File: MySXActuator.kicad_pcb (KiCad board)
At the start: 2 copper layers, 26.4 x 38.1 mm, 23 parts, among them Q1 2N7002, Q2 IRF530, Q3 IRF530, Q4 2N7002, U1 AP63205WU, X1 FE10-2, X2 MKDSN1,5/6-5,08

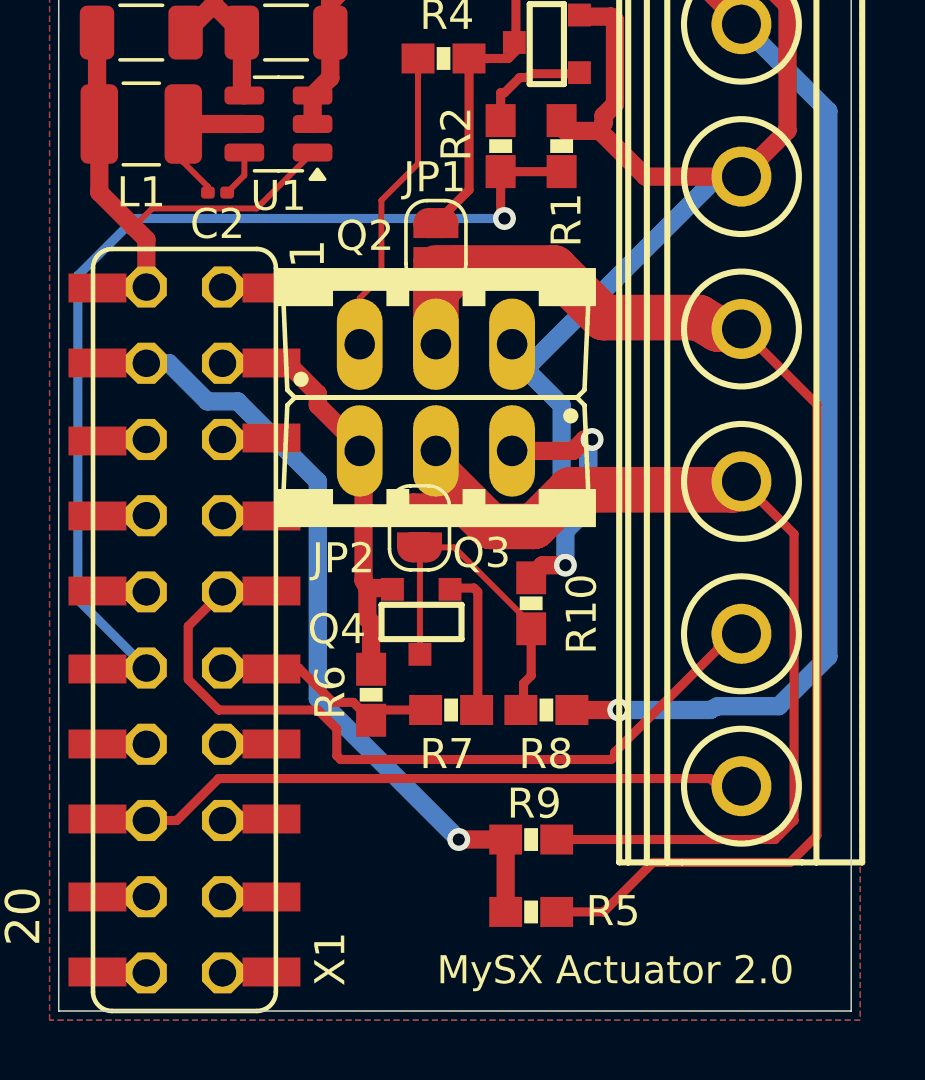
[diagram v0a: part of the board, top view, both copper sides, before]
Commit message: change C2 footprint from 0201 to 0402
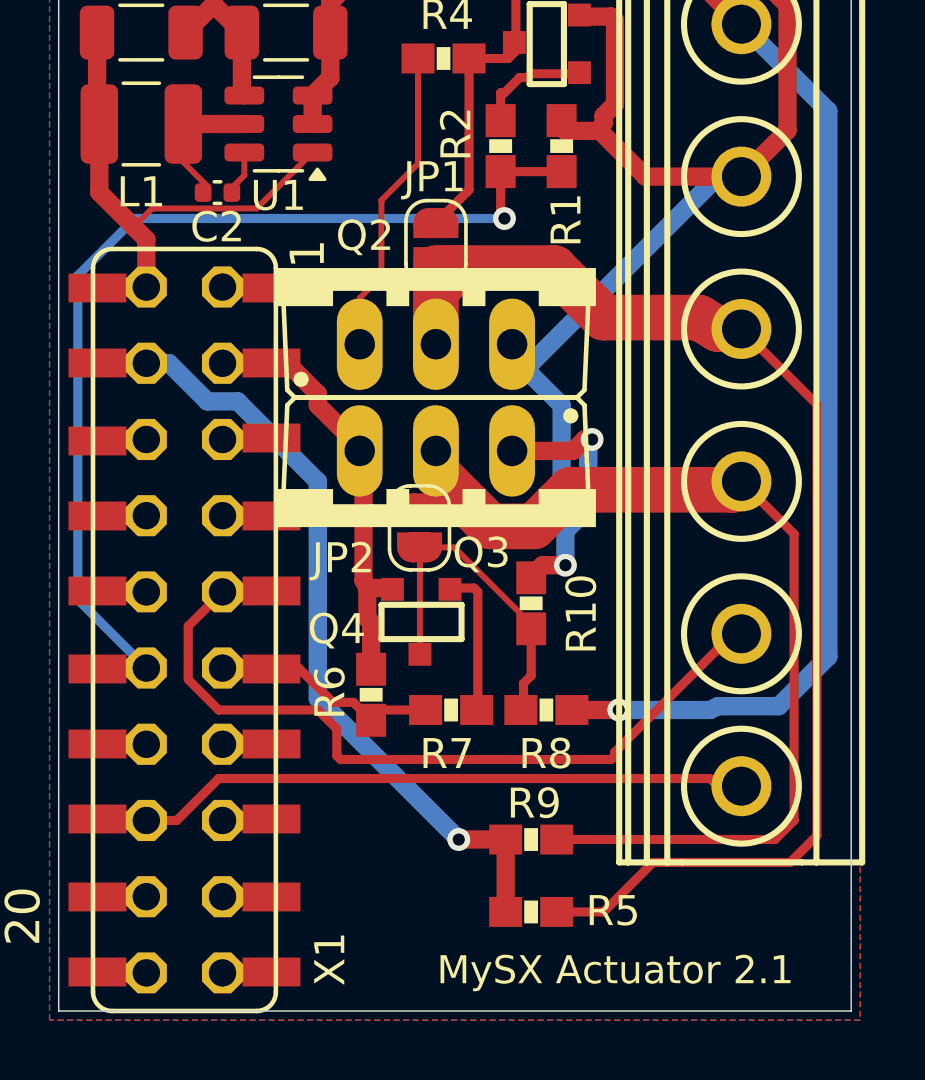
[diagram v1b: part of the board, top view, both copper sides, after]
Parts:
- C2: footprint Capacitor_SMD:C_0201_0603Metric -> Capacitor_SMD:C_0402_1005Metric
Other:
- board text added: "MySX Actuator 2.1"
- board text removed: "MySX Actuator 2.0"
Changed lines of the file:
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@@
       (net 9 "Net-(JP2-A)") (pinfunction "2") (pintype "passive") (solder_mask_margin 0.0762) (thermal_bridge_angle 0))
   )
-  (footprint "Capacitor_SMD:C_0201_0603Metric" (layer "F.Cu")
+  (footprint "Capacitor_SMD:C_0402_1005Metric" (layer "F.Cu")
     (at 140.586 96.774 180)
-    (descr "Capacitor SMD 0201 (0603 Metric), square (rectangular) end terminal, IPC_7351 nominal, (Body size source: https://www.vishay.com/docs/20052/crcw0201e3.pdf), generated with kicad-footprint-generator")
+    (descr "Capacitor SMD 0402 (1005 Metric), square (rectangular) end terminal, IPC_7351 nominal, (Body size source: IPC-SM-782 page 76, https://www.pcb-3d.com/wordpress/wp-content/uploads/ipc-sm-782a_amendment_1_and_2.pdf), generated with kicad-footprint-generator")
     (tags "capacitor")
     (property "Sheetfile" "MySXActuator.kicad_sch")
@@
     (property "ki_keywords" "cap capacitor")
     (attr smd)
-    (fp_text reference "C2" (at 0 -1.05) (layer "F.SilkS")
+    (fp_text reference "C2" (at 0 -1.16 180) (layer "F.SilkS")
         (effects (font (size 1 1) (thickness 0.15)))
     )
-    (fp_text value "100n" (at 0 1.05) (layer "F.Fab")
+    (fp_text value "100n" (at 0 1.16 180) (layer "F.Fab")
         (effects (font (size 1 1) (thickness 0.15)))
     )
-    (fp_text user "${REFERENCE}" (at 0 -0.68) (layer "F.Fab")
+    (fp_text user "${REFERENCE}" (at 0 0 180) (layer "F.Fab")
         (effects (font (size 0.25 0.25) (thickness 0.04)))
     )
-    (fp_line (start -0.7 -0.35) (end 0.7 -0.35)
-      (stroke (width 0.05) (type solid)) (layer "F.CrtYd"))
-    (fp_line (start -0.7 0.35) (end -0.7 -0.35)
-      (stroke (width 0.05) (type solid)) (layer "F.CrtYd"))
-    (fp_line (start 0.7 -0.35) (end 0.7 0.35)
-      (stroke (width 0.05) (type solid)) (layer "F.CrtYd"))
-    (fp_line (start 0.7 0.35) (end -0.7 0.35)
-      (stroke (width 0.05) (type solid)) (layer "F.CrtYd"))
-    (fp_line (start -0.3 -0.15) (end 0.3 -0.15)
-      (stroke (width 0.1) (type solid)) (layer "F.Fab"))
-    (fp_line (start -0.3 0.15) (end -0.3 -0.15)
-      (stroke (width 0.1) (type solid)) (layer "F.Fab"))
-    (fp_line (start 0.3 -0.15) (end 0.3 0.15)
-      (stroke (width 0.1) (type solid)) (layer "F.Fab"))
-    (fp_line (start 0.3 0.15) (end -0.3 0.15)
-      (stroke (width 0.1) (type solid)) (layer "F.Fab"))
-    (pad "" smd roundrect (at -0.345 0 180) (size 0.318 0.36) (layers "F.Paste") (roundrect_rratio 0.25))
-    (pad "" smd roundrect (at 0.345 0 180) (size 0.318 0.36) (layers "F.Paste") (roundrect_rratio 0.25))
-    (pad "1" smd roundrect (at -0.32 0 180) (size 0.46 0.4) (layers "F.Cu" "F.Mask") (roundrect_rratio 0.25)
+    (fp_line (start -0.107836 -0.36) (end 0.107836 -0.36)
+      (stroke (width 0.12) (type solid)) (layer "F.SilkS"))
+    (fp_line (start -0.107836 0.36) (end 0.107836 0.36)
+      (stroke (width 0.12) (type solid)) (layer "F.SilkS"))
+    (fp_line (start -0.91 -0.46) (end 0.91 -0.46)
+      (stroke (width 0.05) (type solid)) (layer "F.CrtYd"))
+    (fp_line (start -0.91 0.46) (end -0.91 -0.46)
+      (stroke (width 0.05) (type solid)) (layer "F.CrtYd"))
+    (fp_line (start 0.91 -0.46) (end 0.91 0.46)
+      (stroke (width 0.05) (type solid)) (layer "F.CrtYd"))
+    (fp_line (start 0.91 0.46) (end -0.91 0.46)
+      (stroke (width 0.05) (type solid)) (layer "F.CrtYd"))
+    (fp_line (start -0.5 -0.25) (end 0.5 -0.25)
+      (stroke (width 0.1) (type solid)) (layer "F.Fab"))
+    (fp_line (start -0.5 0.25) (end -0.5 -0.25)
+      (stroke (width 0.1) (type solid)) (layer "F.Fab"))
+    (fp_line (start 0.5 -0.25) (end 0.5 0.25)
+      (stroke (width 0.1) (type solid)) (layer "F.Fab"))
+    (fp_line (start 0.5 0.25) (end -0.5 0.25)
+      (stroke (width 0.1) (type solid)) (layer "F.Fab"))
+    (pad "1" smd roundrect (at -0.48 0 180) (size 0.56 0.62) (layers "F.Cu" "F.Paste" "F.Mask") (roundrect_rratio 0.25)
       (net 29 "Net-(U1-BST)") (pintype "passive"))
-    (pad "2" smd roundrect (at 0.32 0 180) (size 0.46 0.4) (layers "F.Cu" "F.Mask") (roundrect_rratio 0.25)
+    (pad "2" smd roundrect (at 0.48 0 180) (size 0.56 0.62) (layers "F.Cu" "F.Paste" "F.Mask") (roundrect_rratio 0.25)
       (net 30 "Net-(U1-SW)") (pintype "passive"))
-    (model "${KICAD6_3DMODEL_DIR}/Capacitor_SMD.3dshapes/C_0201_0603Metric.wrl"
+    (model "${KICAD6_3DMODEL_DIR}/Capacitor_SMD.3dshapes/C_0402_1005Metric.wrl"
       (offset (xyz 0 0 0))
       (scale (xyz 1 1 1))
@@
   (gr_line (start 161.7091 85.9536) (end 135.2931 85.9536)
     (stroke (width 0.05) (type solid)) (layer "Edge.Cuts"))
-  (gr_text "MySX Actuator 2.0" (at 159.8041 122.1486) (layer "F.SilkS")
+  (gr_text "MySX Actuator 2.1" (at 159.8041 122.1486) (layer "F.SilkS")
     (effects (font (size 0.93472 0.93472) (thickness 0.08128)) (justify right top))
   )

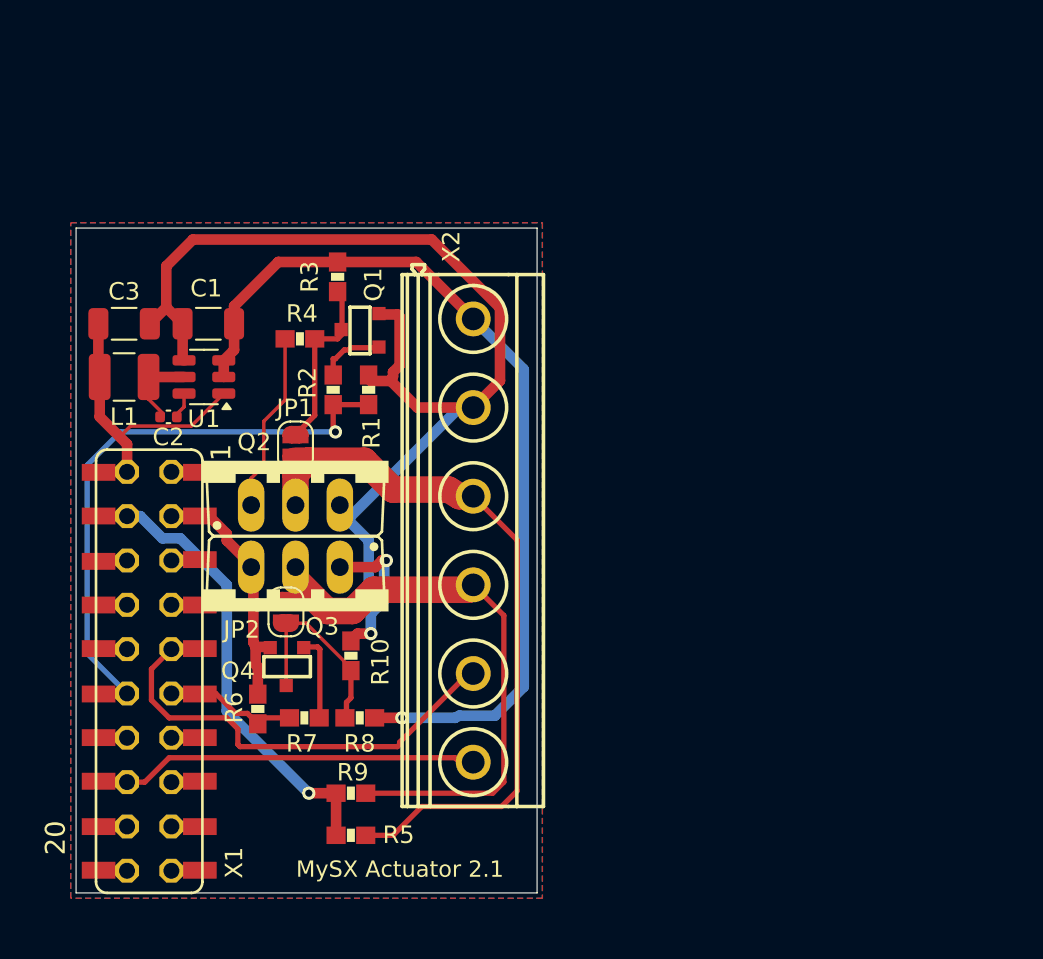
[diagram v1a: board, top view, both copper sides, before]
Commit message: refactor schematic to use kicad native symbols and footprints
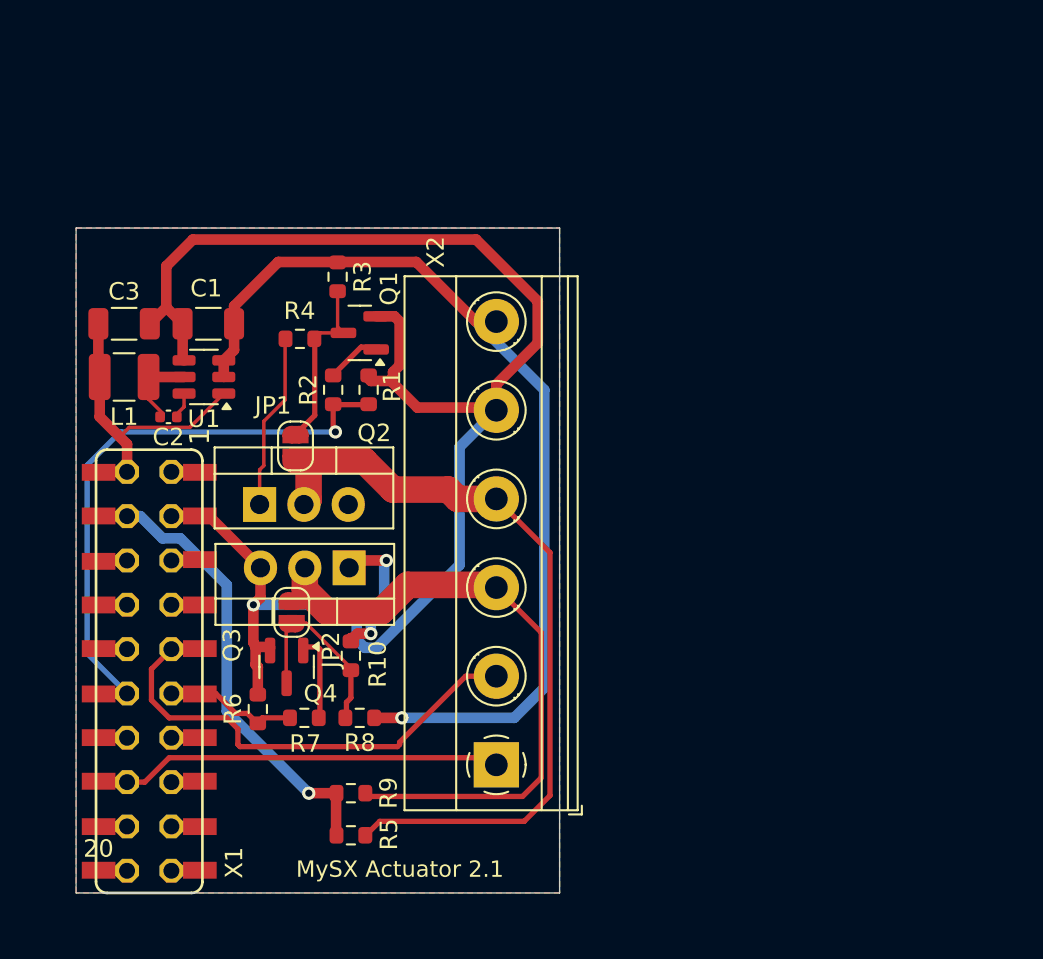
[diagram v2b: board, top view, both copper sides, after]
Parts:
- C1: value 10u -> 10u/50V
- Q1, Q4: footprint MySXActuator:SOT-23 -> Package_TO_SOT_SMD:SOT-23
- Q2, Q3: value IRF530 -> IRF540N; footprint MySXActuator:TO220BV -> Package_TO_SOT_THT:TO-220-3_Vertical
- R1, R10, R2, R3, R4, R5, R6, R7, R8, R9: footprint MySXActuator:0603-RES -> Resistor_SMD:R_0603_1608Metric
- X1: value FE10-2 -> ~
- X2: value MKDSN1,5/6-5,08 -> ~; footprint MySXActuator:MKDSN1,5_6-5,08 -> TerminalBlock_Phoenix:TerminalBlock_Phoenix_MKDS-1,5-6-5.08_1x06_P5.08mm_Horizontal
- moved X2 12.9 mm to (159.4, 116.7), turned to 90 degrees
- moved Q3 3.96 mm to (150.9, 105.4)
- moved Q2 3.24 mm to (145.8, 101.8)
- moved JP2 0.33 mm to (147.7, 108.0)
- moved Q1 0.17 mm to (151.5, 92.0), turned to 180 degrees
- turned Q4 to -90 degrees
- turned R1 to 90 degrees
- turned R10 to 90 degrees
- turned R3 to -90 degrees
- turned R4 to 180 degrees
- turned R5 to 0 degrees
- turned R6 to 90 degrees
- turned R8 to 180 degrees
- turned R9 to 0 degrees
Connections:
- net /D10_A4 renamed D10_A4
- net /D11_MOSI renamed D11_MOSI
- net /D12_MISO renamed D12_MISO
- net /D13_SCK renamed D13_SCK
- net /D14_CS renamed D14_CS
- net /D1_TX renamed D1_TX
- net /D2_RX renamed D3_RX
- net /D3_INT renamed D3_INT
- net /D7_SCL renamed D7_SCL
- net /D8_SDA renamed D8_SDA
- net /LEGACY_ID renamed LEGACY_ID
- net /RST renamed RST
- net /VCC renamed VCC
- net /VRAW renamed VRAW
- C1 pad 1: /Vin -> VIN
- JP1 pad 2: /LED1 -> LED1
- JP2 pad 2: /LED2 -> LED2
- R1 pad 1: GND -> D5_PWM
- R1 pad 2: /D5_PWM -> GND
- R10 pad 1: Net-(Q3-PadG) -> Net-(JP2-A)
- R10 pad 2: Net-(JP2-A) -> Net-(Q3-G)
- R2 pad 1: /D5_PWM -> D5_PWM
- R3 pad 1: Net-(JP1-A) -> VIN
- R3 pad 2: /Vin -> Net-(JP1-A)
- R4 pad 1: Net-(Q2-PadG) -> Net-(JP1-A)
- R4 pad 2: Net-(JP1-A) -> Net-(Q2-G)
- R5 pad 1: /LED1 -> VCCIO
- R5 pad 2: /VCCIO -> LED1
- R6 pad 1: GND -> D6_PWM
- R6 pad 2: /D6_PWM -> GND
- R7 pad 1: /D6_PWM -> D6_PWM
- R8 pad 1: Net-(JP2-A) -> VIN
- R8 pad 2: /Vin -> Net-(JP2-A)
- R9 pad 1: /LED2 -> VCCIO
- R9 pad 2: /VCCIO -> LED2
- U1 pad 2: /Vin -> VIN
- U1 pad 3: /Vin -> VIN
- X1 pad 11: /D6_PWM -> D6_PWM
- X1 pad 12: /D5_PWM -> D5_PWM
- X1 pad 16: /D9_A3 -> D9_A3
- X1 pad 4: /VCCIO -> VCCIO
- X1 pad 9: /D4_INT -> D4_INT
- X2 pad 1: /Vin -> D9_A3
- X2 pad 2: GND -> D4_INT
- X2 pad 3: /LED1 -> LED2
- X2 pad 4: /LED2 -> LED1
- X2 pad 5: /D4_INT -> GND
- X2 pad 6: /D9_A3 -> VIN
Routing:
- net VIN: track 0.00 -> 55.1 mm, vias 0 -> 1
- net /Vin: track 52.0 -> 0.00 mm, vias 1 -> 0
- net LED1: track 0.00 -> 44.8 mm
- net /LED1: track 41.5 -> 0.00 mm
- net LED2: track 0.00 -> 37.8 mm
- net /LED2: track 34.6 -> 0.00 mm
- net D5_PWM: track 0.00 -> 32.7 mm, vias 0 -> 1
- net /D5_PWM: track 32.7 -> 0.00 mm, vias 1 -> 0
- net D4_INT: track 0.00 -> 26.5 mm
- net /D4_INT: track 25.6 -> 0.00 mm
- net VCCIO: track 0.00 -> 25.2 mm, vias 0 -> 1
- net /VCCIO: track 25.2 -> 0.00 mm, vias 1 -> 0
- net D9_A3: track 0.00 -> 21.9 mm
- net /D9_A3: track 20.5 -> 0.00 mm
- net Net-(Q2-PadG): track 10.3 -> 0.00 mm
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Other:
- board size 26.4 x 38.1 mm -> 27.7 x 38.1 mm

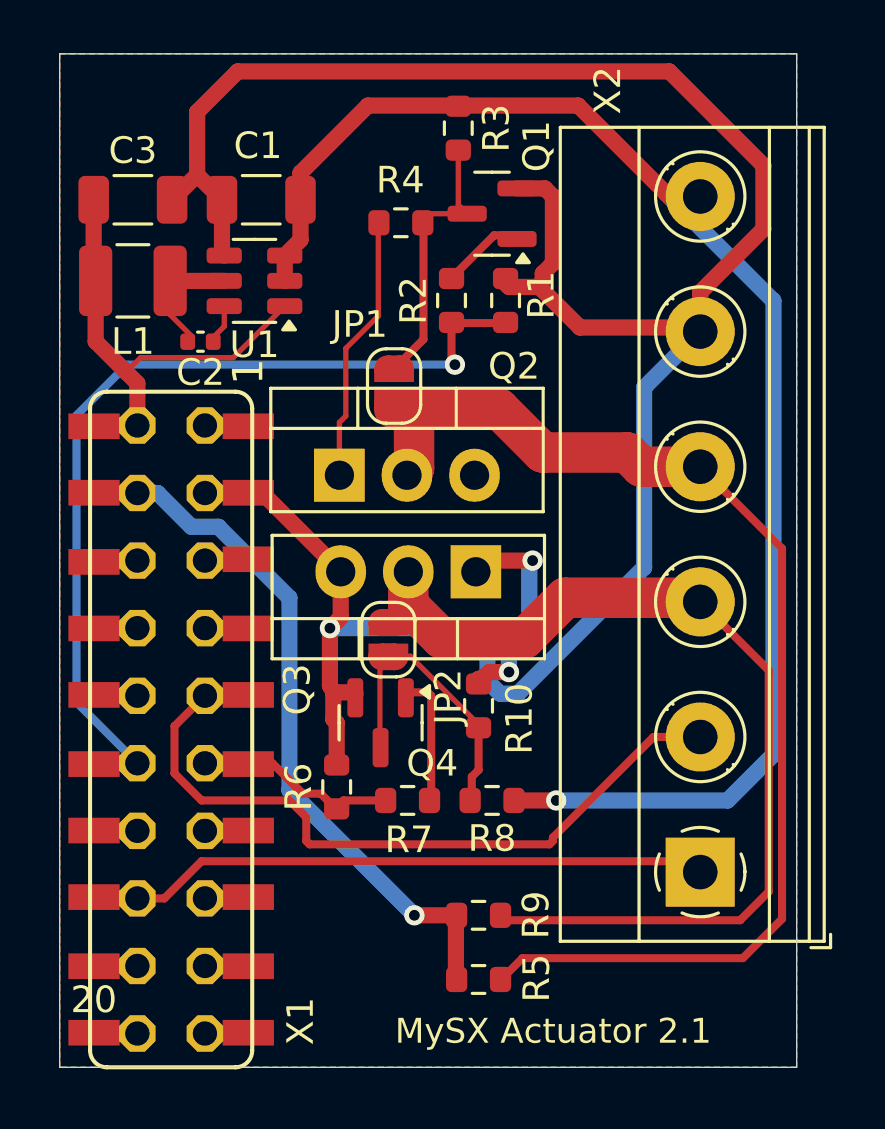
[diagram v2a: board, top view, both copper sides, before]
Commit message: add reverse polarity protection and overvoltage protection for input pins
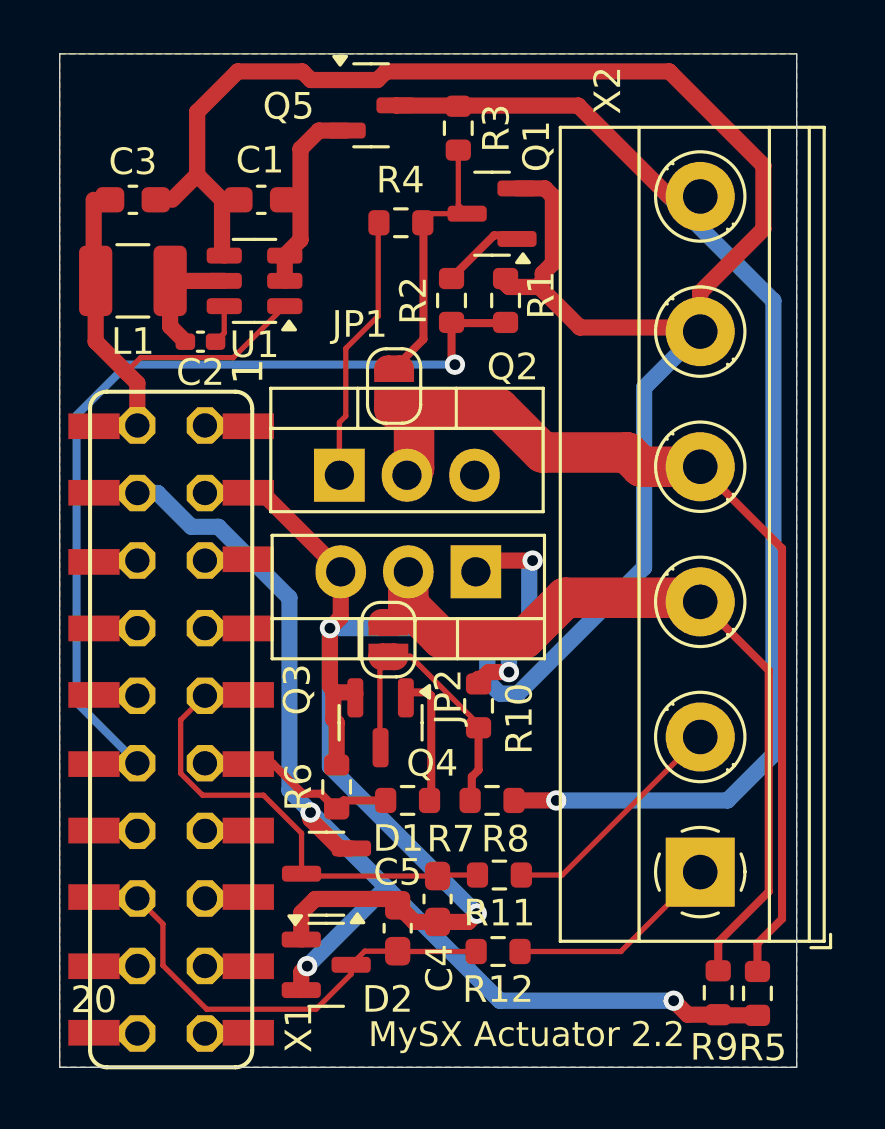
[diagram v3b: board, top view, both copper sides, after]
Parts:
- added C4: 10n, Capacitor_SMD:C_0603_1608Metric_Pad1.08x0.95mm_HandSolder, F.Cu at (149.5, 117.7)
- added C5: 10n, Capacitor_SMD:C_0603_1608Metric_Pad1.08x0.95mm_HandSolder, F.Cu at (148.0, 118.8)
- added D1: BAT54S, Package_TO_SOT_SMD:SOT-23, F.Cu at (145.3, 116.8)
- added D2: BAT54S, Package_TO_SOT_SMD:SOT-23, F.Cu at (145.3, 120.2)
- added Q5: ~, Package_TO_SOT_SMD:SOT-23, F.Cu at (147.0, 87.9)
- added R11: 2k, Resistor_SMD:R_0603_1608Metric, F.Cu at (151.8, 116.8)
- added R12: 2k, Resistor_SMD:R_0603_1608Metric, F.Cu at (151.8, 119.7)
- C1: footprint Capacitor_SMD:C_1206_3216Metric -> Capacitor_SMD:C_0603_1608Metric_Pad1.08x0.95mm_HandSolder
- C2: value 100n -> 100n/50V; footprint Capacitor_SMD:C_0402_1005Metric -> Capacitor_SMD:C_0402_1005Metric_Pad0.74x0.62mm_HandSolder
- C3: value 22u -> 10u; footprint Capacitor_SMD:C_1206_3216Metric -> Capacitor_SMD:C_0603_1608Metric_Pad1.08x0.95mm_HandSolder
- moved R5 10.5 mm to (161.5, 121.3), turned to 90 degrees
- moved R9 9.47 mm to (160.1, 121.2), turned to 90 degrees
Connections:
- C1 pad 1: VIN -> Net-(Q5-S)
- U1 pad 2: VIN -> Net-(Q5-S)
- U1 pad 3: VIN -> Net-(Q5-S)
- X2 pad 1: D9_A3 -> SW2
- X2 pad 2: D4_INT -> SW1
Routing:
- net GND: track 91.6 -> 113.2 mm, vias 1 -> 2
- net VCCIO: track 25.2 -> 43.2 mm, vias 1 -> 3
- net D4_INT: track 26.5 -> 17.0 mm
- net LED1: track 44.8 -> 35.7 mm
- net VIN: track 55.1 -> 46.1 mm
- net SW1: track 0.00 -> 8.87 mm
- net SW2: track 0.00 -> 8.01 mm
- net Net-(Q5-S): track 0.00 -> 7.21 mm
- net LED2: track 37.8 -> 31.0 mm
- net D9_A3: track 21.9 -> 16.5 mm
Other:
- board text added: "MySX Actuator 2.2"
- board text removed: "MySX Actuator 2.1"
